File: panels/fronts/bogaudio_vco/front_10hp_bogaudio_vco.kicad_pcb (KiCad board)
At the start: 2 copper layers, 50.5 x 128.5 mm, 8 parts

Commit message: Rev 3 boards complete - probably
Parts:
- removed the + at (88.6, 129.2)
- removed the + at (88.6, 107.9)
- removed the + at (88.6, 86.6)
- removed the + at (88.6, 65.3)
- moved + 5.75 mm to (89.7, 123.6)
- moved + 4.76 mm to (89.7, 103.3)
- moved + 3.88 mm to (89.7, 83.0)
- moved + 2.91 mm to (89.7, 62.6)
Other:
- outline, holes or cut-outs redrawn
- net class Default removed
- rule pad_to_mask_clearance: 0 -> 0.05

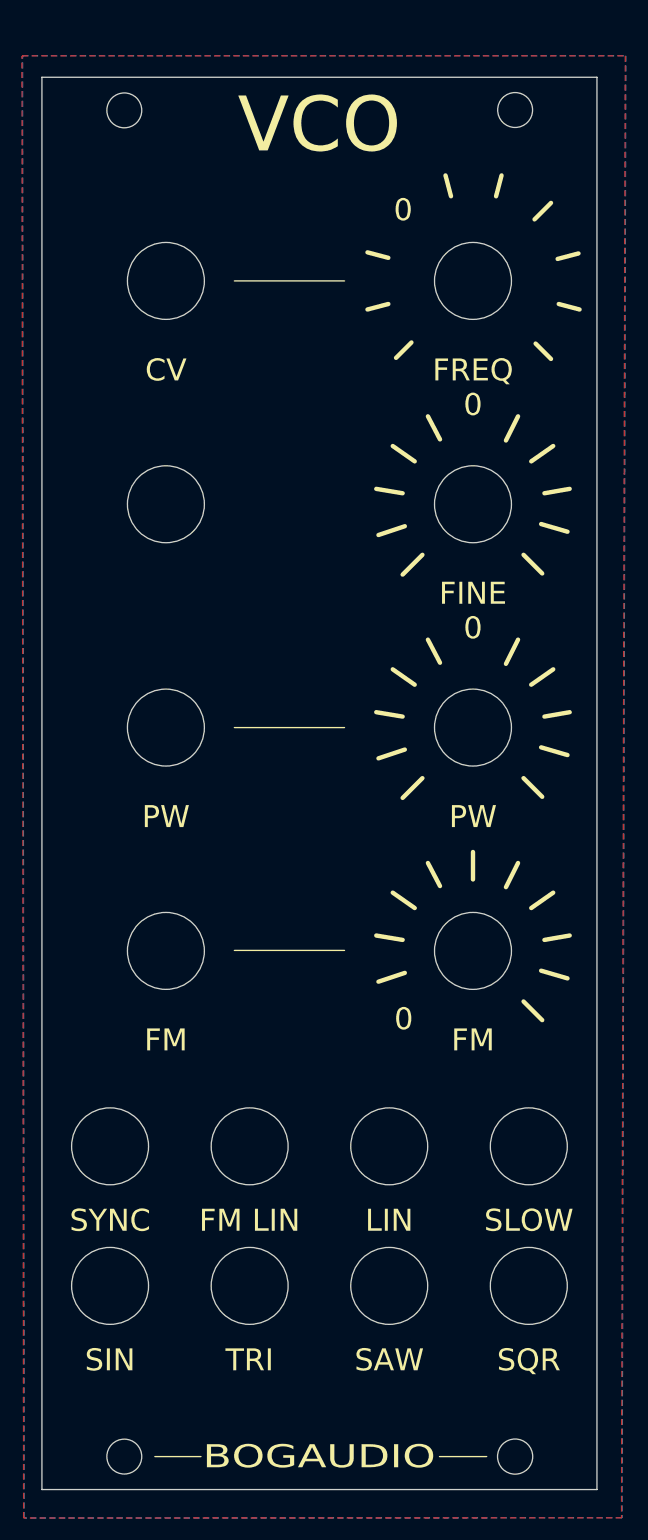
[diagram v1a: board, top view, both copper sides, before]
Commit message: R3 PCB and front panel
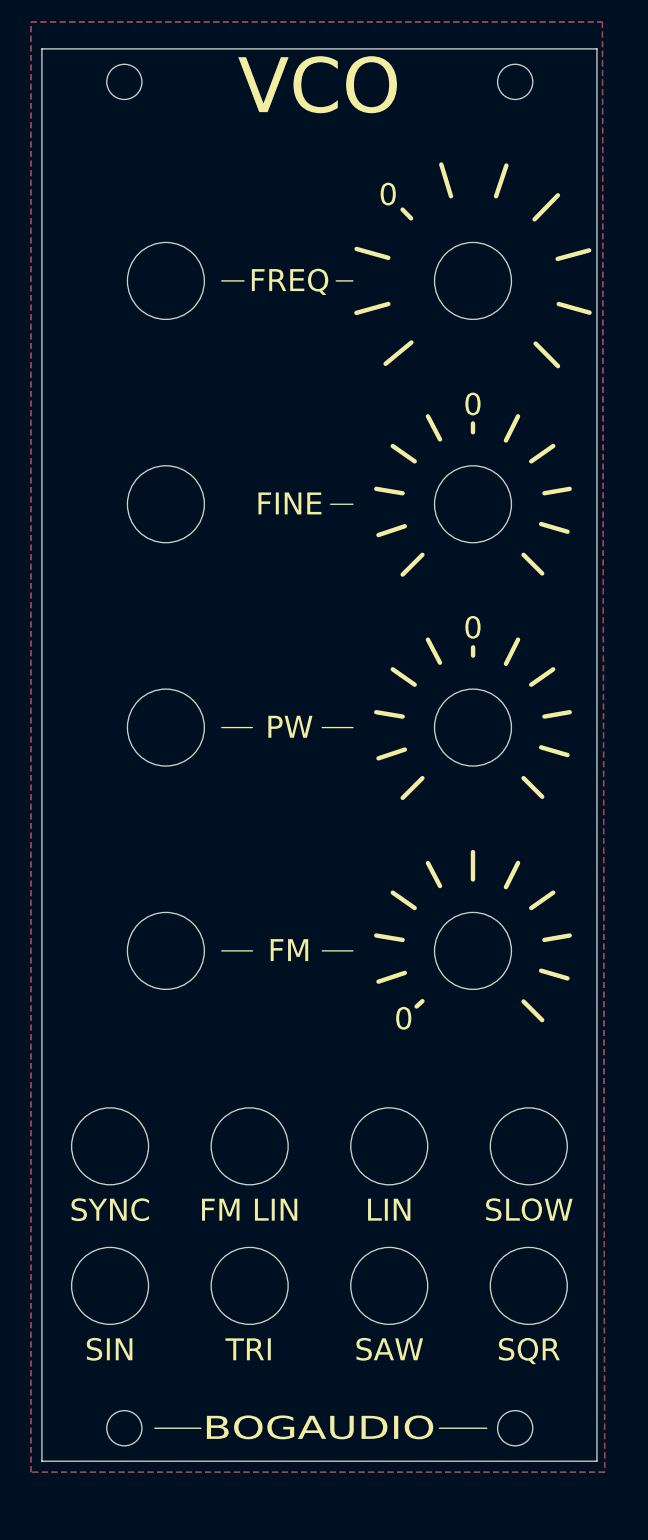
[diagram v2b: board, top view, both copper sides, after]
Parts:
- added +: PW, Decals:Scale_11pt_13mm_0-5, B.Cu at (89.7, 62.6)
- added +: PW, Decals:Scale_11pt_13mm_0-5, B.Cu at (89.7, 83.0)
- added +: PW, Decals:Scale_11pt_13mm_0-5, B.Cu at (61.8, 62.6)
- added +: PW, Decals:Scale_11pt_13mm_0-5, B.Cu at (61.8, 103.3)
- added +: PW, Decals:Scale_11pt_13mm_0-5, B.Cu at (89.7, 103.3)
- added +: PW, Decals:Scale_11pt_13mm_0-5, B.Cu at (61.8, 83.0)
- added +: PW, Decals:Scale_11pt_13mm_0-5, B.Cu at (89.7, 123.6)
- added +: PW, Decals:Scale_11pt_13mm_0-5, B.Cu at (61.8, 123.6)
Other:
- outline, holes or cut-outs redrawn
- board text added: "1"
- board text added: "2"
- board text added: "ATTACK"
- board text added: "DECAY"
- board text added: "DUAL ADSR"
- board text added: "FINE"
- board text added: "FREQ"
- board text added: "GATE"
- board text added: "OUT"
- board text added: "RELEASE"
- board text added: "SUSTAIN"
- board text removed: "CV"
- board text removed: "JLCJLCJLCJLC"

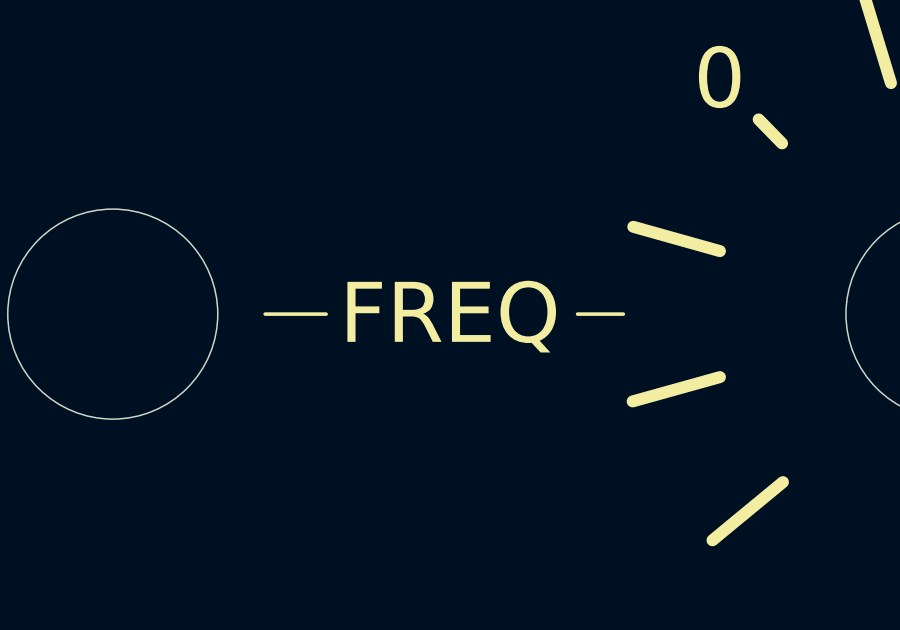
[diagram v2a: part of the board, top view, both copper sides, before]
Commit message: Fixes polyphonic mode by removing loading polyphony from snapshot. Module may have any quantity of MIDI inputs and outputs defined. Rationalise port names to use "output" or "input" and not "out" or "in". Rationalise use of "freq", "frequency", etc.
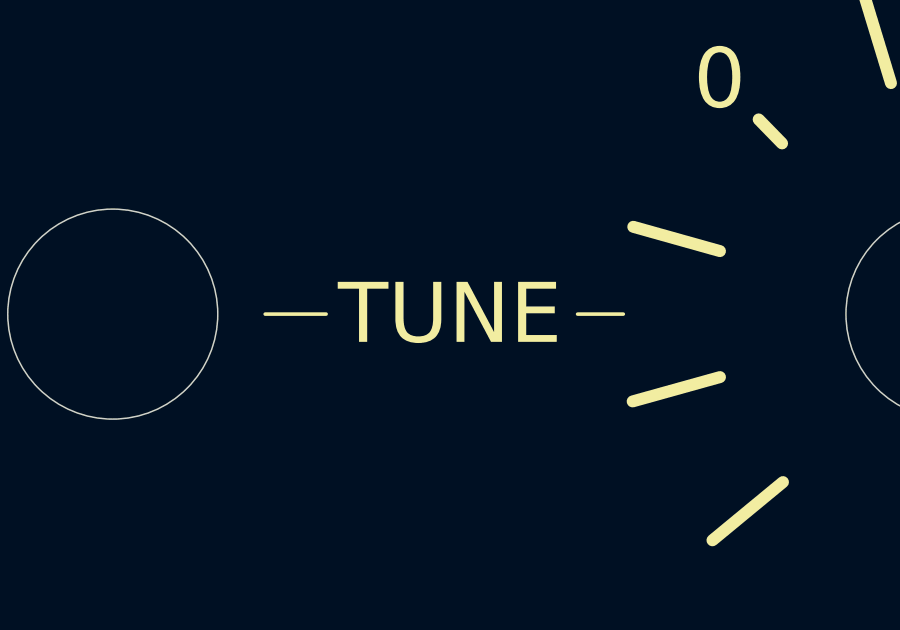
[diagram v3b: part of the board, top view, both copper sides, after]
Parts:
- +: value FREQ -> V/OCT
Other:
- board text added: "TUNE"
- board text removed: "FREQ"
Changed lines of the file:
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@@
 			)
 		)
-		(property "Value" "FREQ"
+		(property "Value" "V/OCT"
 			(at 0 10.34 0)
 			(layer "F.SilkS")
@@
 		)
 	)
-	(gr_text "FREQ"
+	(gr_text "TUNE"
 		(at 73.0265 62.63 0)
 		(layer "F.SilkS")
